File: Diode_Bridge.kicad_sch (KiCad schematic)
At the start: 0 parts

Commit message: Video Commit
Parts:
- added D1, D2: D, symbol Device:D
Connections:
- net GND: now also D2.1 (K)
- net Vin: now also D1.2 (A)
- new net: D1.1 (K), D2.2 (A)

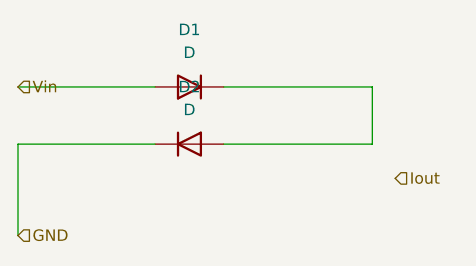
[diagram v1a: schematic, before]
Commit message: deleted diodes
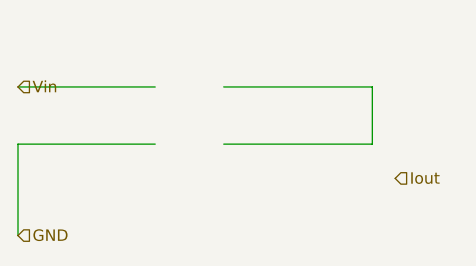
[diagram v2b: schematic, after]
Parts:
- removed D1, D2: D, symbol Device:D
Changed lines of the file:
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@@
-		)
-	)
-	(symbol
-		(lib_id "Device:D")
-		(at 104.14 63.5 180)
-		(unit 1)
-		(body_style 1)
-		(exclude_from_sim no)
-		(in_bom yes)
-		(on_board yes)
-		(in_pos_files yes)
-		(dnp no)
-		(fields_autoplaced yes)
-		(property "Reference" "D1"
-			(at 104.14 57.15 0)
-			(show_name no)
-			(do_not_autoplace no)
-			(effects
-				(font
-					(size 1.27 1.27)
-				)
-			)
-		)
-		(property "Value" "D"
-			(at 104.14 59.69 0)
-			(show_name no)
-			(do_not_autoplace no)
-			(effects
-				(font
-					(size 1.27 1.27)
-				)
-			)
-		)
-		(property "Footprint" ""
-			(at 104.14 63.5 0)
-			(hide yes)
-			(show_name no)
-			(do_not_autoplace no)
-			(effects
-				(font
-					(size 1.27 1.27)
-				)
-			)
-		)
-		(property "Datasheet" ""
-			(at 104.14 63.5 0)
-			(hide yes)
-			(show_name no)
-			(do_not_autoplace no)
-			(effects
-				(font
-					(size 1.27 1.27)
-				)
-			)
-		)
-		(property "Description" "Diode"
-			(at 104.14 63.5 0)
-			(hide yes)
-			(show_name no)
-			(do_not_autoplace no)
-			(effects
-				(font
-					(size 1.27 1.27)
-				)
-			)
-		)
-		(property "Sim.Device" "D"
-			(at 104.14 63.5 0)
-			(hide yes)
-			(show_name no)
-			(do_not_autoplace no)
-			(effects
-				(font
-					(size 1.27 1.27)
-				)
-			)
-		)
-		(property "Sim.Pins" "1=K 2=A"
-			(at 104.14 63.5 0)
-			(hide yes)
-			(show_name no)
-			(do_not_autoplace no)
-			(effects
-				(font
-					(size 1.27 1.27)
-				)
-			)
-		)
-		(pin "2"
-		)
-		(pin "1"
-		)
-		(instances
-			(project "Solar_Battery"
-				(path "/6805959e-39bb-4644-b93e-3970e29fedc0/a320594e-eb17-43a9-8193-2f75b3718179/66c5df4f-46ad-4d4f-997c-052ec03a6539"
-					(reference "D1")
-					(unit 1)
-				)
-			)
-		)
-	)
-	(symbol
-		(lib_id "Device:D")
-		(at 104.14 69.85 0)
-		(unit 1)
-		(body_style 1)
-		(exclude_from_sim no)
-		(in_bom yes)
-		(on_board yes)
-		(in_pos_files yes)
-		(dnp no)
-		(fields_autoplaced yes)
-		(property "Reference" "D2"
-			(at 104.14 63.5 0)
-			(show_name no)
-			(do_not_autoplace no)
-			(effects
-				(font
-					(size 1.27 1.27)
-				)
-			)
-		)
-		(property "Value" "D"
-			(at 104.14 66.04 0)
-			(show_name no)
-			(do_not_autoplace no)
-			(effects
-				(font
-					(size 1.27 1.27)
-				)
-			)
-		)
-		(property "Footprint" ""
-			(at 104.14 69.85 0)
-			(hide yes)
-			(show_name no)
-			(do_not_autoplace no)
-			(effects
-				(font
-					(size 1.27 1.27)
-				)
-			)
-		)
-		(property "Datasheet" ""
-			(at 104.14 69.85 0)
-			(hide yes)
-			(show_name no)
-			(do_not_autoplace no)
-			(effects
-				(font
-					(size 1.27 1.27)
-				)
-			)
-		)
-		(property "Description" "Diode"
-			(at 104.14 69.85 0)
-			(hide yes)
-			(show_name no)
-			(do_not_autoplace no)
-			(effects
-				(font
-					(size 1.27 1.27)
-				)
-			)
-		)
-		(property "Sim.Device" "D"
-			(at 104.14 69.85 0)
-			(hide yes)
-			(show_name no)
-			(do_not_autoplace no)
-			(effects
-				(font
-					(size 1.27 1.27)
-				)
-			)
-		)
-		(property "Sim.Pins" "1=K 2=A"
-			(at 104.14 69.85 0)
-			(hide yes)
-			(show_name no)
-			(do_not_autoplace no)
-			(effects
-				(font
-					(size 1.27 1.27)
-				)
-			)
-		)
-		(pin "2"
-		)
-		(pin "1"
-		)
-		(instances
-			(project "Solar_Battery"
-				(path "/6805959e-39bb-4644-b93e-3970e29fedc0/a320594e-eb17-43a9-8193-2f75b3718179/66c5df4f-46ad-4d4f-997c-052ec03a6539"
-					(reference "D2")
-					(unit 1)
-				)
-			)
 		)
 	)
